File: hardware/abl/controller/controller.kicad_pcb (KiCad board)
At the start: 4 copper layers, 56.2 x 74 mm, 38 parts, among them IC1 TCA6408ARSVR, IC2 TCA6408ARSVR, IC3 VEML6040A3OG, IC4 TXB0104RUT, J1 SFW20S-2STE1LF, J2 Conn_02x05_Odd_Even, J3 Conn_02x05_Odd_Even, J4 PRT-14417, J5 Conn_02x05_Odd_Even, Q2 AO3401A, Q4 AO3401A, U1 INA219AxD

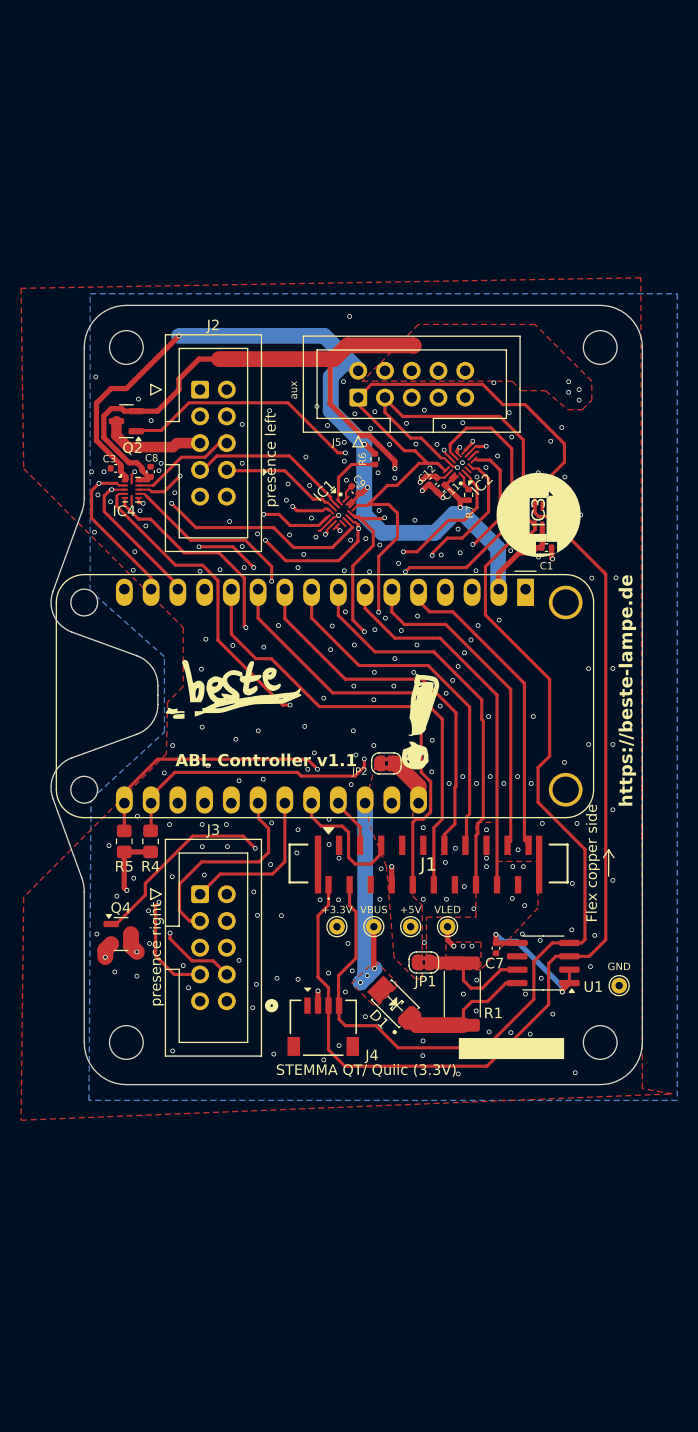
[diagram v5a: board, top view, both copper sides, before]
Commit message: Extended with wings to attach presence sensors directly. Removed distinction between VLED and 5V. Much cleanup.
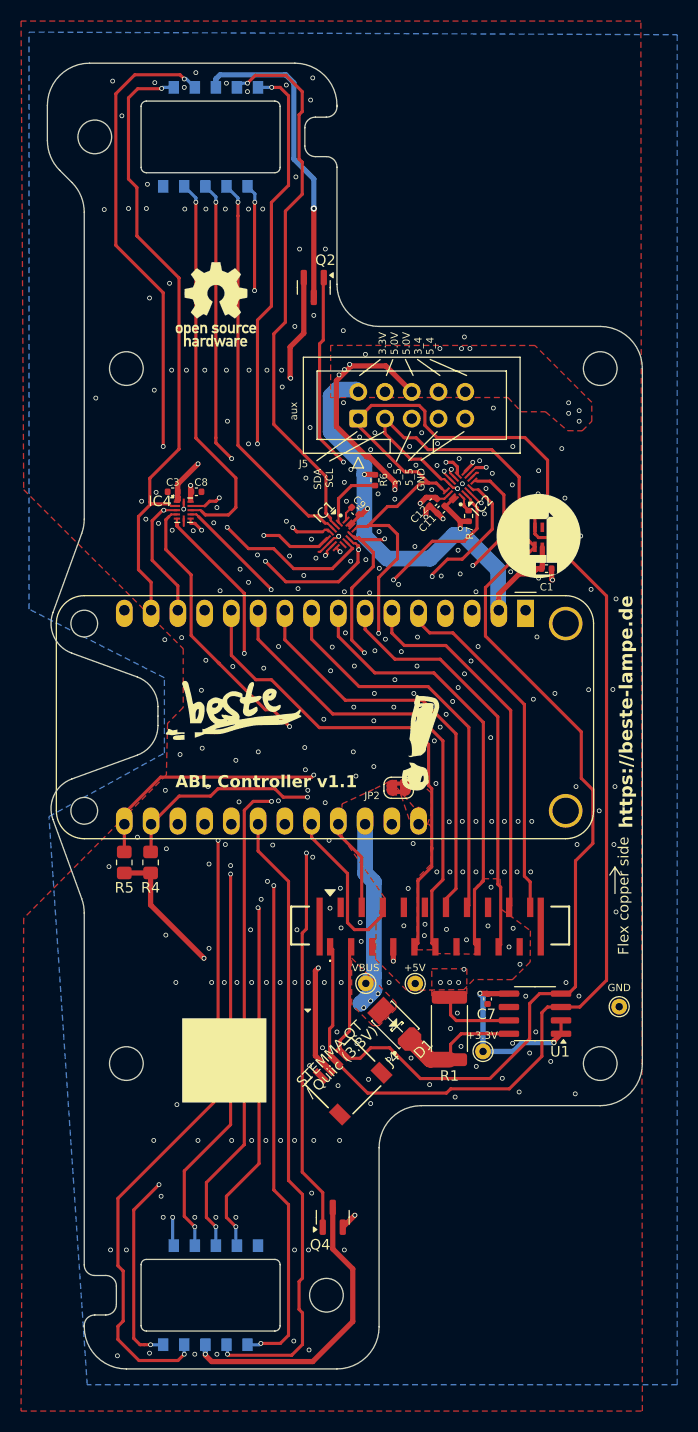
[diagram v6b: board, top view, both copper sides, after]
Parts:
- removed JP1: SolderJumper_2_Bridged, Jumper:SolderJumper-2_P1.3mm_Bridged2Bar_RoundedPad1.0x1.5mm
- removed TP5: TestPoint, TestPoint:TestPoint_THTPad_D1.5mm_Drill0.7mm
- added H5: MountingHole, MountingHole:MountingHole_3.2mm_M3_DIN965, F.Cu at (64.0, 35.0)
- added H6: MountingHole, MountingHole:MountingHole_3.2mm_M3_DIN965, F.Cu at (86.0, 145.0)
- added REF**: OSHW-Logo_7.5x8mm_SilkScreen, Symbol:OSHW-Logo_7.5x8mm_SilkScreen, F.Cu at (75.5, 50.9)
- J2, J3: footprint Connector_IDC:IDC-Header_2x05_P2.54mm_Vertical -> Own footprints:Dual Row Inverted Thru Board Card Edge Connector 02x05 Kyocera AVX 009159010603906; moved to B.Cu
- moved J3 38.1 mm to (73.0, 145.0)
- moved Q4 33.6 mm to (86.6, 137.6), turned to 90 degrees
- moved J2 24.2 mm to (77.0, 35.0), turned to 180 degrees
- moved Q2 21.9 mm to (84.8, 49.3), turned to -90 degrees
- moved TP2 18.2 mm to (100.9, 121.8)
- moved J1 5.89 mm to (95.8, 110.0)
- moved C3 5.85 mm to (71.4, 68.7)
- moved J4 5.50 mm to (88.0, 124.6), turned to 45 degrees
- moved TP4 5.44 mm to (89.7, 115.4)
- moved TP3 5.42 mm to (94.4, 115.4)
- moved IC4 5.32 mm to (72.5, 70.5)
- moved C7 4.88 mm to (101.3, 116.9)
- moved U1 4.88 mm to (105.8, 118.3)
- moved C8 4.75 mm to (73.7, 68.7), turned to 180 degrees
- moved R1 3.49 mm to (97.7, 119.7)
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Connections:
- J1 pad 16: +4V -> +5V
- J1 pad 19: +4V -> +5V
- J2 pad 1: /TX_L -> /FX_5_0
- J2 pad 10: / FX_5_1 -> GND
- J2 pad 2: GND -> /FX_5_1
- J2 pad 3: /RX_L -> /FX_3_0
- J2 pad 4: /RX_L_5 -> /FX_3_1
- J2 pad 7: /FX_3_0 -> /RX_L
- J2 pad 8: /FX_3_1 -> /RX_L_5
- J2 pad 9: /FX_5_0 -> /TX_L
- J3 pad 1: /TX_R -> /FX_5_2
- J3 pad 10: /FX_5_3 -> GND
- J3 pad 2: GND -> /FX_5_3
- J3 pad 3: /RX_R -> /FX_3_2
- J3 pad 4: /RX_R_5 -> /FX_3_3
- J3 pad 7: /FX_3_2 -> /RX_R
- J3 pad 8: /FX_3_3 -> /RX_R_5
- J3 pad 9: /FX_5_2 -> /TX_R
- J4 pad 5: (no net) -> GND
- J4 pad 6: (no net) -> GND
- J5 pad 4: +4V -> +5V
- R1 pad 2: +4V -> +5V
- U1 pad 7: +4V -> +5V
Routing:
- net /FX_5_1: track 0.00 -> 50.9 mm, vias 0 -> 3
- net /FX_5_2: track 67.0 -> 105.3 mm, vias 1 -> 3
- net /FX_3_2: track 58.4 -> 96.4 mm, vias 2 -> 3
- net /FX_3_0: track 15.5 -> 52.4 mm, vias 0 -> 1
- net /RX_R: track 56.5 -> 92.4 mm, vias 1 -> 2
- net /TX_R: track 53.9 -> 89.7 mm, vias 1 -> 3
- net /FX_5_0: track 37.8 -> 73.1 mm, vias 1 -> 3
- net /RX_L: track 29.1 -> 62.8 mm, vias 1 -> 3
- net /TX_L: track 31.7 -> 60.1 mm
- net +3.3V: track 158.9 -> 186.9 mm
- net /FX_5_3: track 67.2 -> 93.8 mm, vias 1 -> 2
- net /FX_3_1: track 12.4 -> 37.4 mm, vias 0 -> 1
- net /TX_L_5: track 10.1 -> 34.1 mm, vias 0 -> 3
- net /RX_L_5: track 14.1 -> 37.3 mm
- net Net-(J2-Pin_5): track 9.92 -> 30.3 mm, vias 0 -> 1
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- added copper zone on F.Cu, net +BATT
- removed copper zone on In2.Cu, net +3.3V
- removed copper zone on F.Cu, net +4V
- removed copper zone on In2.Cu, net +4V
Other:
- board size 56.2 x 74 mm -> 56.5 x 124 mm
- board text added: "3.3V 5.0V 5.0V 3_4 5_4"
- board text added: "3_5 5_5 GND"
- board text added: "SDA SCL"
- board text removed: "VLED"
- board text removed: "presence left"
- board text removed: "presence right"

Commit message: Many, many minor updates to the big PCBs, and a few simple helper PCBs.
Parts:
- added J6: Conn_01x10_Pin, Connector_PinHeader_2.54mm:PinHeader_1x10_P2.54mm_Vertical, F.Cu at (91.0, 77.4)
- added J7: Conn_01x10_Pin, Connector_PinHeader_2.54mm:PinHeader_1x10_P2.54mm_Vertical, F.Cu at (90.9, 102.8)
- moved IC1 3.82 mm to (84.2, 70.6)
- moved C9 3.82 mm to (85.6, 68.4)
- moved R4 2.78 mm to (69.3, 106.7)
- moved R5 2.78 mm to (66.8, 106.7)
- moved JP2 1.22 mm to (91.6, 96.8)
- moved J5 0.85 mm to (89.4, 61.0)
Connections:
- J4 pad 5: GND -> (no net)
- J4 pad 6: GND -> (no net)
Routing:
- net VBUS: track 20.0 -> 34.1 mm
- net /SCL: track 183.4 -> 194.8 mm, vias 4 -> 3
- net /SDA: track 193.5 -> 203.5 mm
- net +5V: track 122.0 -> 112.1 mm, vias 25 -> 21
- net /GP_INT: track 37.6 -> 33.2 mm
- net /EN_UART: track 20.8 -> 16.7 mm
- net /FX_3_1: track 37.4 -> 33.4 mm
- net /FX_3_0: track 52.4 -> 49.0 mm
- net Net-(IC1-~{RESET}): track 6.27 -> 9.60 mm
- net /RX_R_5: track 78.2 -> 81.3 mm
- net /FX_3_3: track 81.9 -> 79.0 mm
- net +3.3V: track 186.9 -> 189.2 mm
- net /FX_3_2: track 96.4 -> 97.9 mm
- net /TX_R_5: track 76.9 -> 78.2 mm
- net /EN_LED: track 15.7 -> 17.0 mm
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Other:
- board text added: "3.3V"
- board text added: "3_4"
- board text added: "3_5"
- board text added: "5.0V"
- board text added: "5_4"
- board text added: "5_5"
- board text added: "SCL"
- board text added: "SDA"
- board text removed: "3.3V 5.0V 5.0V 3_4 5_4"
- board text removed: "3_5 5_5 GND"
- board text removed: "SDA SCL"
- board text removed: "aux"

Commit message: Many small adjustments for the next production run.
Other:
- board text added: "ABL Controller v1.2"
- board text removed: "ABL Controller v1.1"
